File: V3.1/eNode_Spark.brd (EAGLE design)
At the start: 30 x 65 mm, 70 parts, among them U1 WM-N-BM-09, U10 OPA344, U2 MCP73831T-2ACI/OT, U3 R8008-33, U5 HTU21DSMD, U6 TMP006, U7 BMP180, U8 USD-SOCKETSMD, U9 MIC9.7MM, X1 USB-MICROB

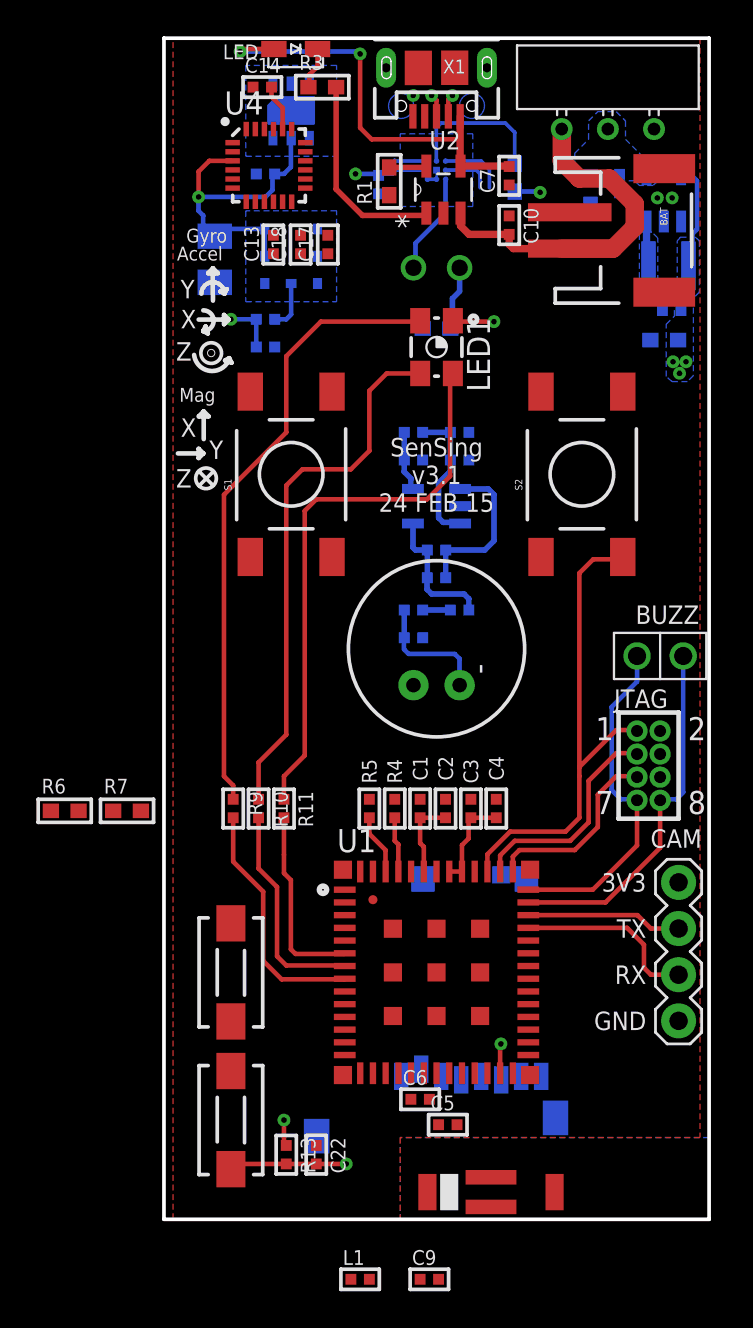
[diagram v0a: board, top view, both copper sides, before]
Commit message: Fully Routed
Fully Routed, DRC checked, Gerbers generated
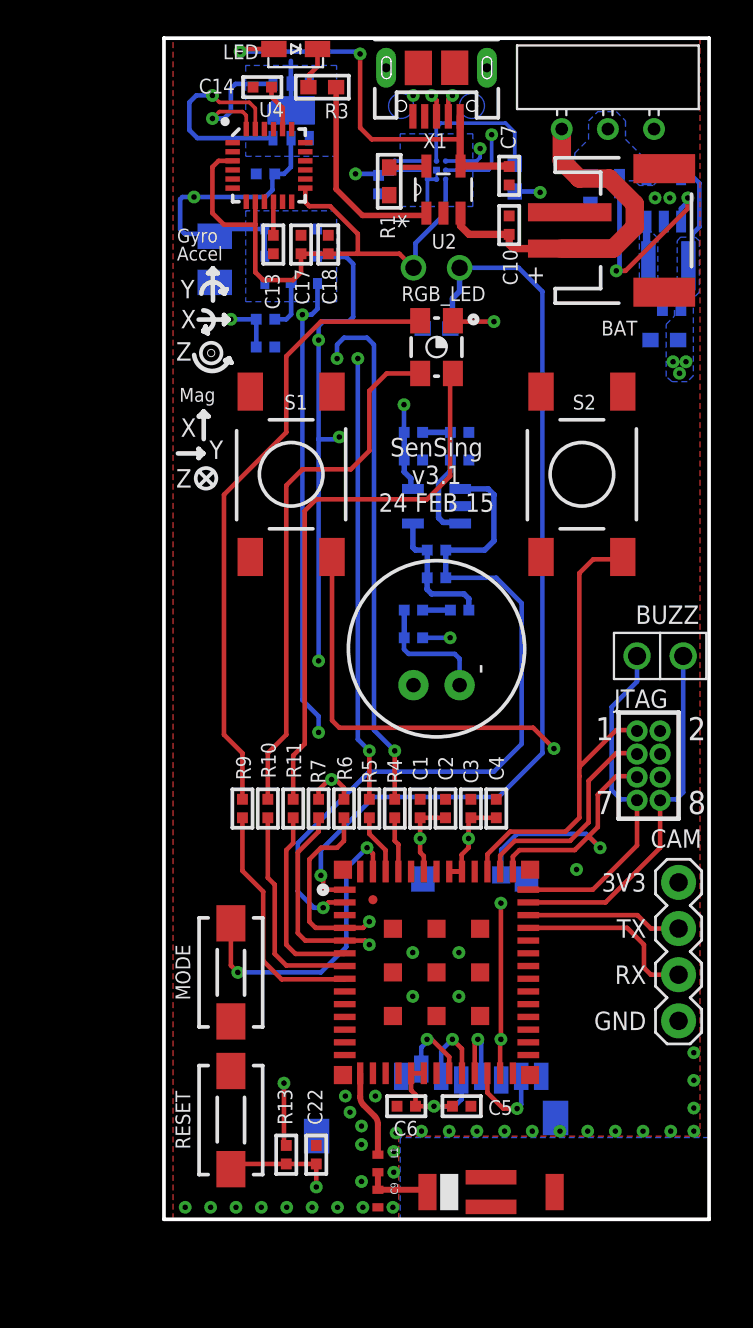
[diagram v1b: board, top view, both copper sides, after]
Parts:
- C9: device rc-master-smd:C0402 -> Spark:R0402_B
- L1: device rc-master-smd:L0402 -> Spark:L0402_B
- R6, R7: device rc-master-smd:R0603 -> rc-master-smd:R0402
- moved R6 15.4 mm to (9.91, 22.6), turned to 270 degrees
- moved R7 10.5 mm to (8.51, 22.6), turned to 90 degrees
- moved L1 6.45 mm to (11.8, 3.07), turned to 270 degrees
- moved C9 5.27 mm to (11.8, 1.14), turned to 270 degrees
- moved C18 1.52 mm to (9.04, 53.6), turned to 270 degrees
- moved C17 1.47 mm to (7.54, 53.6), turned to 270 degrees
- moved C5 1.27 mm to (16.4, 6.22)
- moved C6 0.85 mm to (13.3, 6.22)
- moved R10 0.51 mm to (5.71, 22.6)
- moved R11 0.51 mm to (7.11, 22.6)
- moved R9 0.51 mm to (4.32, 22.6)
- renumbered LED1 to RGB_LED
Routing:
- net SCL: track 2.75 -> 110.9 mm, vias 0 -> 6
- net SDA: track 3.61 -> 95.1 mm, vias 0 -> 5
- net LDR: track 3.55 -> 51.8 mm, vias 0 -> 1
- net +3V3: track 55.6 -> 98.6 mm, vias 9 -> 15
- net N$18: track 5.68 -> 46.5 mm, vias 1 -> 3
- net N$17: track 6.40 -> 42.4 mm, vias 1 -> 3
- net MIC: track 8.92 -> 41.7 mm, vias 0 -> 1
- net PBL/TDI: track 12.1 -> 39.3 mm, vias 0 -> 1
- net !MODE: track 0.00 -> 16.8 mm, vias 0 -> 2
- net ENABLE: track 0.00 -> 11.8 mm, vias 0 -> 2
- net SD_CD/TRST: track 10.6 -> 19.0 mm, vias 0 -> 1
- net !RST: track 41.7 -> 47.2 mm, vias 2 -> 3
- net MISO: track 0.00 -> 4.93 mm, vias 0 -> 1
- net ANT: track 0.00 -> 4.81 mm
- net GND: track 5.04 -> 9.56 mm, vias 3 -> 40
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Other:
- board text added: "+"
- board text added: "MODE"
- board text added: "RESET"
